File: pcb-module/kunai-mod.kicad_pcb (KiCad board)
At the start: 2 copper layers, 22 x 22 mm, 25 parts, among them J1 Outline, J2 SWD, Q1 UM6K33NTN, U1 NCP115AMX330TCG, U2 W25Q16JWXHIQ TR, U3 RP2040, Y1 ABM8-272-T3

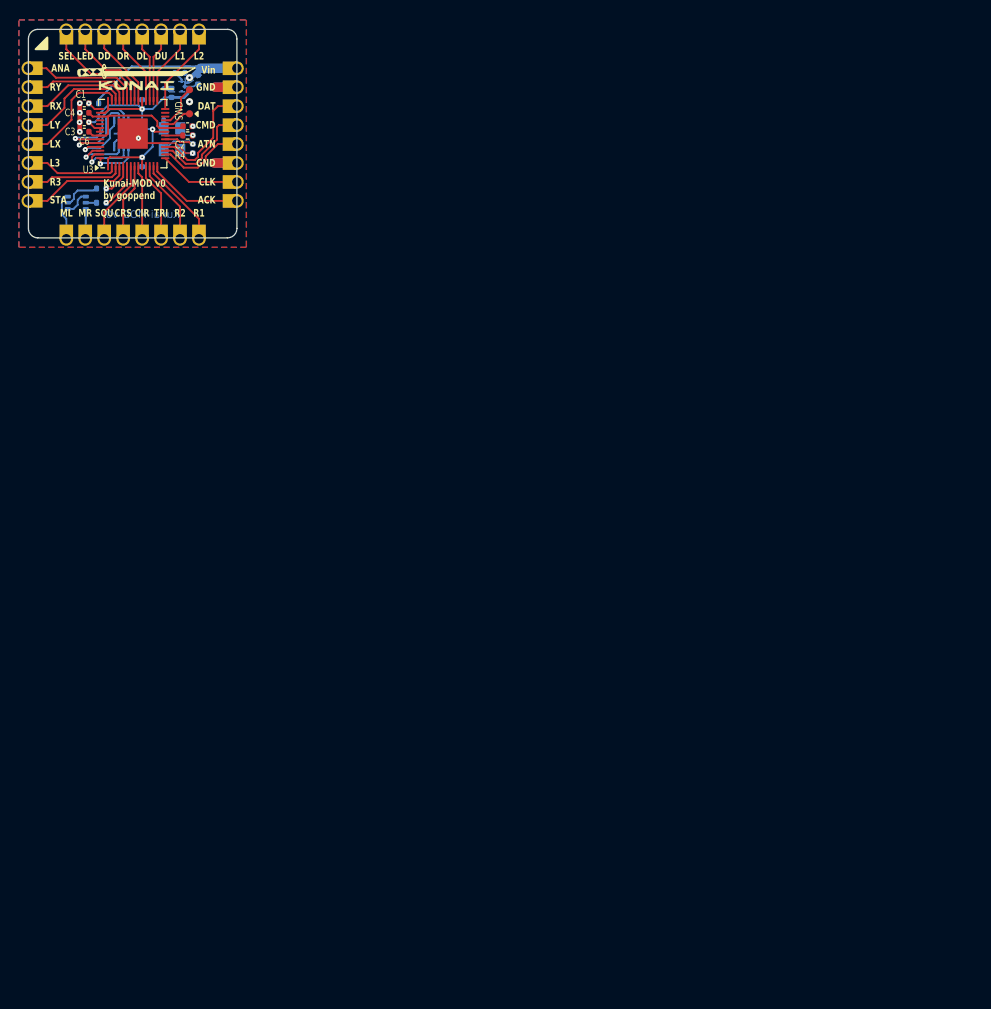
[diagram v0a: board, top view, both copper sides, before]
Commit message: Add footprint and update readme, small tweaks to pcb/schematic.
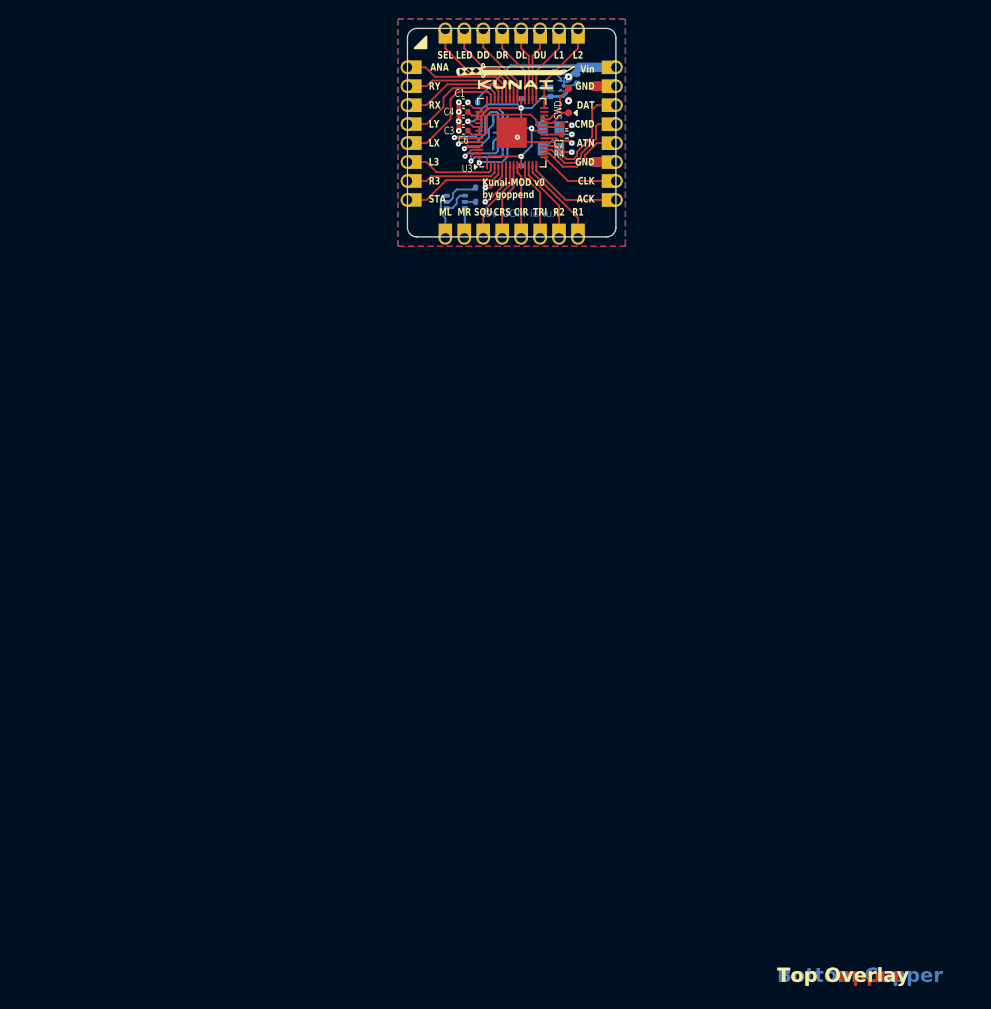
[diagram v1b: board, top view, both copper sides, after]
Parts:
- moved ? 40.0 mm to (140.3, 94.0)
- moved C2 40.0 mm to (145.8, 99.1)
- moved R4 40.0 mm to (145.8, 100.1)
- moved U2 40.0 mm to (138.8, 99.9)
- moved C1 40.0 mm to (134.9, 96.7)
- moved C10 40.0 mm to (140.6, 99.9)
- moved C3 40.0 mm to (134.9, 99.7)
- moved C4 40.0 mm to (134.9, 97.7)
- moved C5 40.0 mm to (141.0, 96.8)
- moved C6 40.0 mm to (134.9, 98.7)
- moved C7 40.0 mm to (141.0, 102.9)
- moved C8 40.0 mm to (146.9, 94.2)
- moved C9 40.0 mm to (144.1, 95.6)
- moved J1 40.0 mm to (140.0, 100.0)
- moved J2 40.0 mm to (146.0, 97.8)
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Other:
- board text added: "Bottom Copper"
- board text added: "Bottom Overlay"
- board text added: "Bottom Paste"
- board text added: "Bottom Soldermask"
- board text added: "Top Copper"
- board text added: "Top Overlay"
- board text added: "Top Paste"
- board text added: "Top Soldermask"
